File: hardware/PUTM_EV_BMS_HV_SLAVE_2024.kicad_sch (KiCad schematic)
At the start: 15 parts, among them J1 L_LTC_CONN, J1 R_LTC_CONN, J3 M80-5100442, J4 M80-5100442, T1 HM1236NL, T3 HM1236NL

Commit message: finished layout
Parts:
- added J5, J6: Conn_01x01_Pin, Connector_Wire:SolderWire-0.1sqmm_1x01_D0.4mm_OD1mm_Relief, symbol Connector:Conn_01x01_Pin
- C6, C7: Manufacturer_Part_Number (none) -> C0603C103J5RACTU; Mouser Part Number (none) -> 80-C0603C103J5R; Mouser Price/Stock (none) -> https://www.mouser.pl/ProductDetail/KEMET/C0603C103J5RACTU?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
- H1, H2, H3, H4: Manufacturer_Name (none) -> --; Manufacturer_Part_Number (none) -> --
- J1: value R_LTC_CONN -> IDC; Manufacturer_Part_Number (none) -> TST-110-01-T-D; Mouser Part Number (none) -> 200-TST11001TD; Mouser Price/Stock (none) -> https://www.mouser.pl/ProductDetail/Samtec/TST-110-01-T-D?q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
- J1: value L_LTC_CONN -> IDC; Manufacturer_Part_Number (none) -> TST-110-01-T-D; Mouser Part Number (none) -> 200-TST11001TD; Mouser Price/Stock (none) -> https://www.mouser.pl/ProductDetail/Samtec/TST-110-01-T-D?q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
- JP1: Manufacturer_Part_Number (none) -> --
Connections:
- net C11+: now also JP1.1 (A), S1.1
- net C2+: no longer JP1.1 (A), S1.1
- net at J3.1 (Pin_1): now also T1.5; no longer T1.4
- net at J3.3 (Pin_3): now also J3.4 (Pin_4), J5.1 (Pin_1); no longer T1.5
- net at T3.4: now also J4.2 (Pin_2); no longer J4.1 (Pin_1)
- net at T3.5: now also J4.1 (Pin_1); no longer J4.3 (Pin_3)
- net C2_SW+ renamed C11_SW+
- new net: J3.2 (Pin_2), T1.4
- new net: J4.3 (Pin_3), J4.4 (Pin_4), J6.1 (Pin_1)

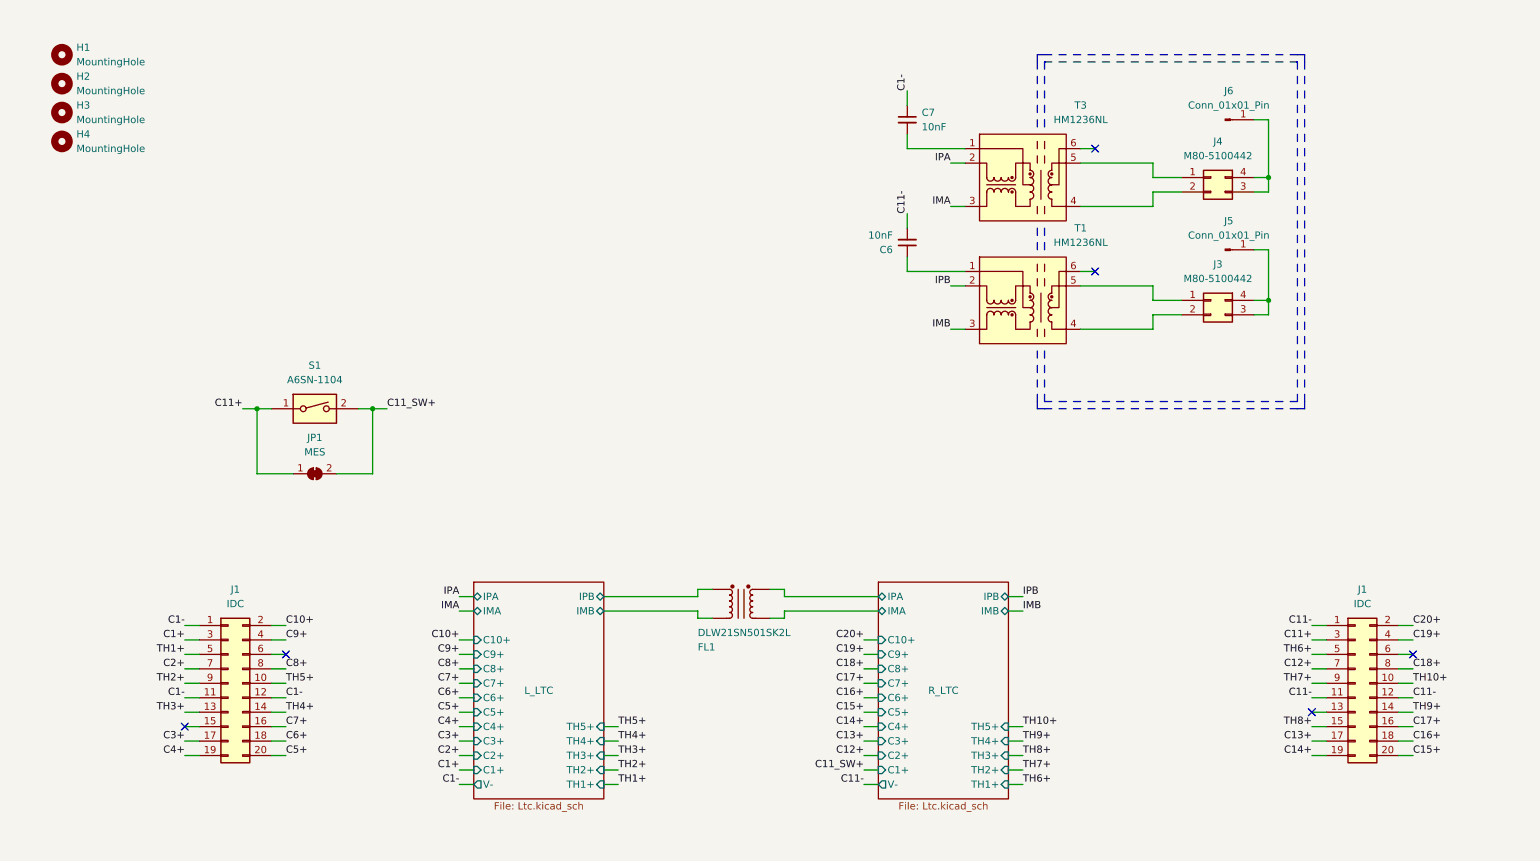
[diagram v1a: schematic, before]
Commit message: change from transformator to capacitive isolation between ltc, change ibias/icmp pin since they are incorrectly connected
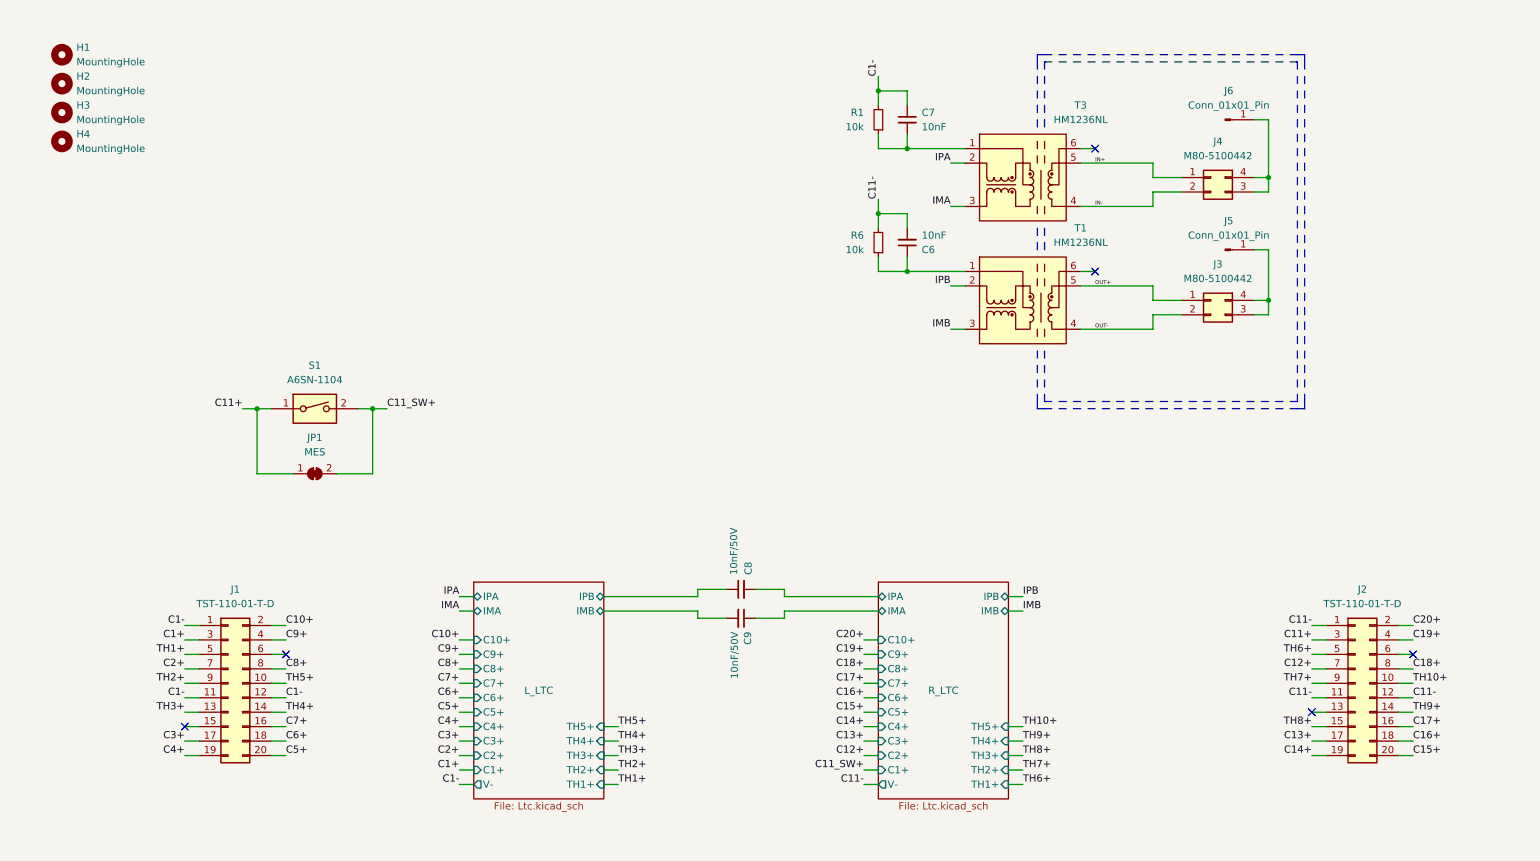
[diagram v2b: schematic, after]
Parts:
- removed FL1: DLW21SN501SK2L, Samacsys:DLW21SN121HQ2L, symbol dlw21sn501sk2l:DLW21SN501SK2L
- added C8, C9: 10nF/50V, Capacitor_SMD:C_0603_1608Metric, symbol PUTM_EV_BMS_HV_Slave_2021-rescue:C_Small-Device
- added R1, R6: 10k, Resistor_SMD:R_0603_1608Metric, symbol Device:R_Small
- J1: value IDC -> TST-110-01-T-D
- J2: renamed from J1; value IDC -> TST-110-01-T-D
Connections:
- net C1-: now also R1.2
- net C11-: now also R6.2
- net L_LTC/IMB: now also C9.2
- net L_LTC/IPB: now also C8.1
- net R_LTC/IMA: now also C9.1
- net R_LTC/IPA: now also C8.2
- net at C7.2, T3.1: now also R1.1
- net at C6.1, T1.1: now also R6.1
- net OUT+: now reaches J3.1 (Pin_1), T1.5
- net OUT-: now reaches J3.2 (Pin_2), T1.4
- net IN-: now reaches J4.2 (Pin_2), T3.4
- net IN+: now reaches J4.1 (Pin_1), T3.5

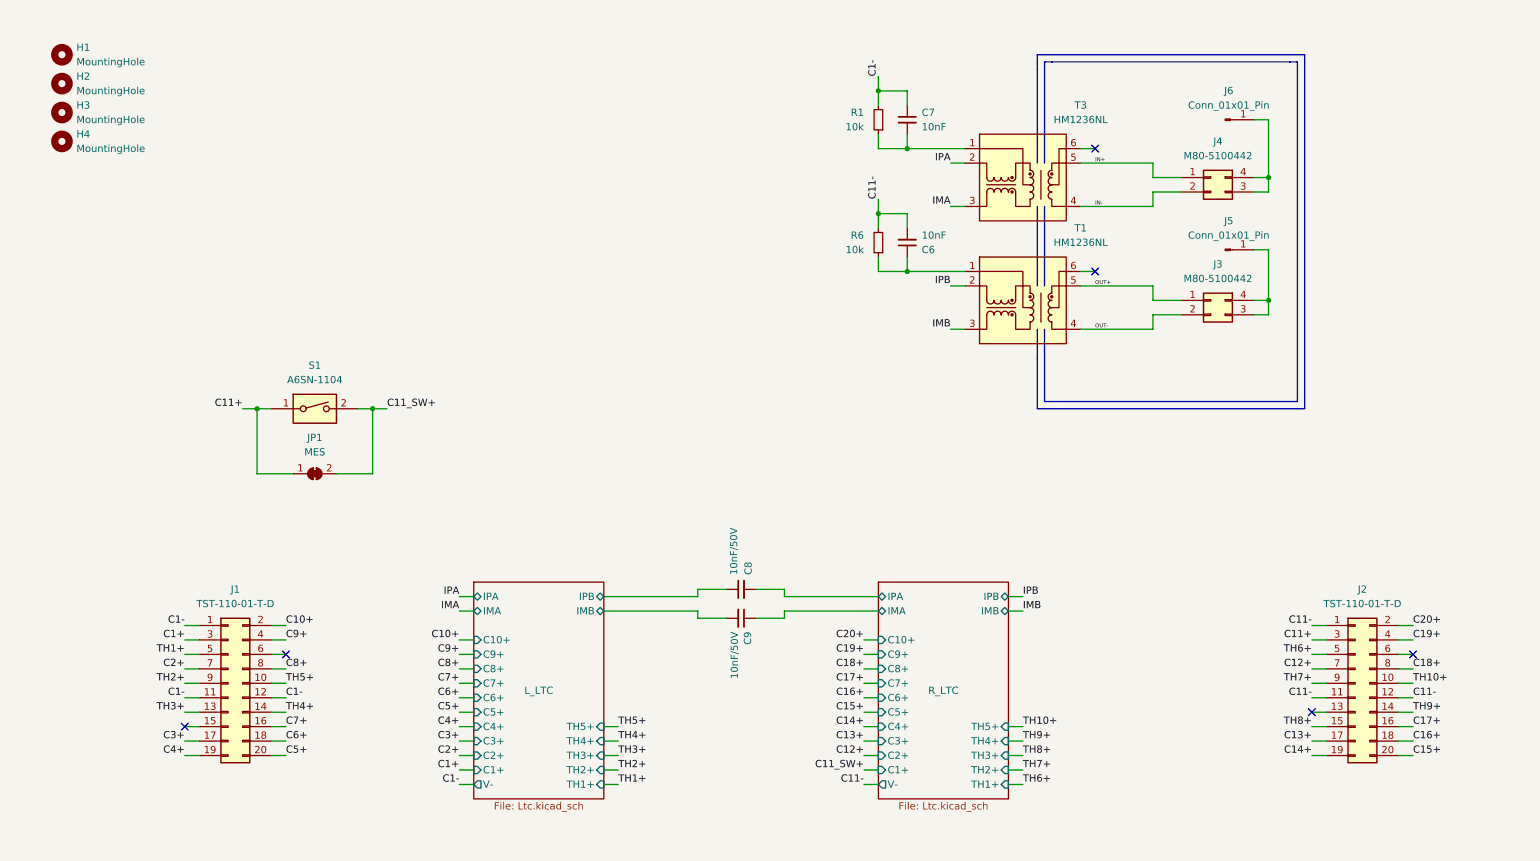
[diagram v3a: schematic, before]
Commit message: added temp disconnect, beautify schematic
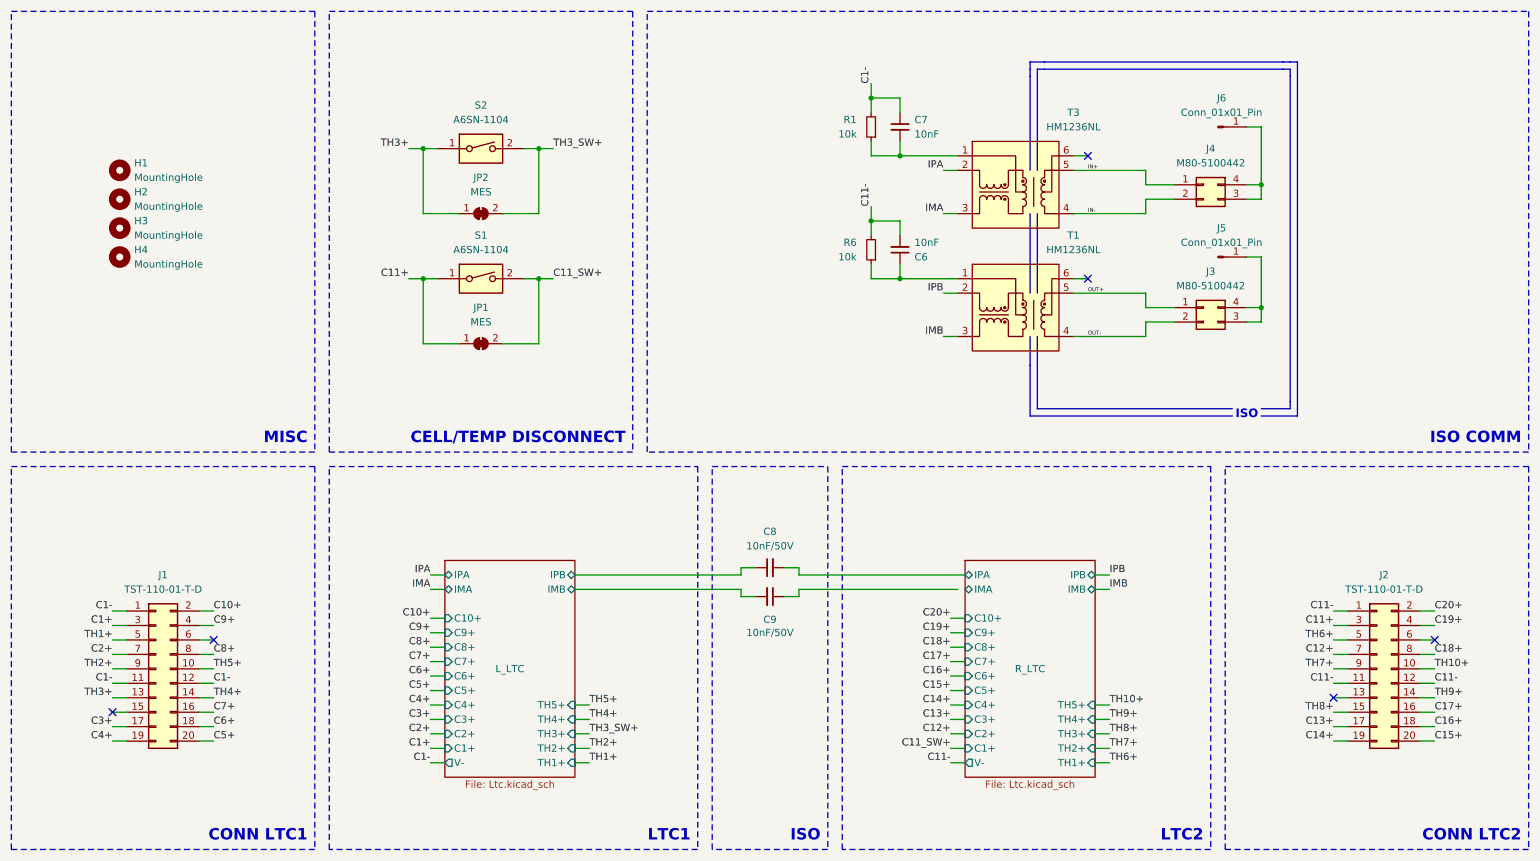
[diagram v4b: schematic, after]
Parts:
- added JP2: MES, Jumper:SolderJumper-2_P1.3mm_Bridged2Bar_RoundedPad1.0x1.5mm, symbol Jumper:SolderJumper_2_Bridged
- added S2: A6SN-1104, Samacsys:A6SN1104, symbol a6sn-1104:A6SN-1104
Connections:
- net R_LTC/IMA: no longer C9.1
- net TH3+: now also JP2.1 (A), S2.1
- new net TH3_SW+: JP2.2 (B), S2.2
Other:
- note added: "CELL/TEMP DISCONNECT"
- note added: "CONN LTC1"
- note added: "CONN LTC2"
- note added: "ISO"
- note added: "ISO COMM"
- note added: "LTC1"
- note added: "LTC2"
- note added: "MISC"
- moved on the sheet: C6, C7, C8, C9, H1, H2, H3, H4, J1, J2, J3, J4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

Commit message: replaced signal transformer with rated capacitors, made the design more general for future use
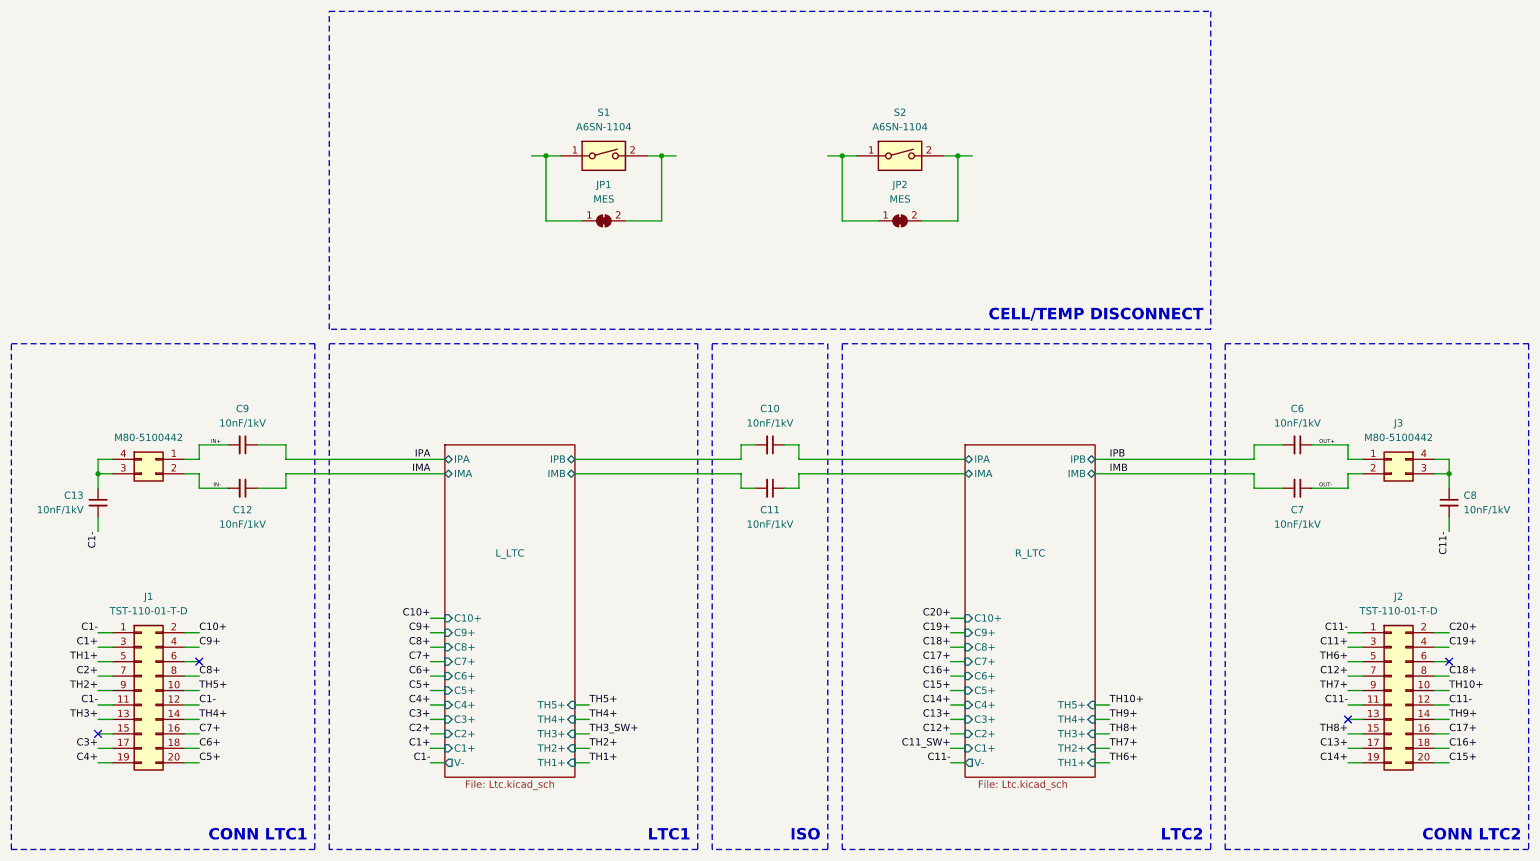
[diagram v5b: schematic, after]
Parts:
- removed C6, C7: 10nF, Capacitor_SMD:C_0603_1608Metric, symbol Device:C_Small
- removed C8, C9: 10nF/50V, Capacitor_SMD:C_0603_1608Metric, symbol PUTM_EV_BMS_HV_Slave_2021-rescue:C_Small-Device
- removed H1, H2, H3, H4: MountingHole, MountingHole:MountingHole_3.2mm_M3, symbol Mechanical:MountingHole
- removed J5, J6: Conn_01x01_Pin, Connector_Wire:SolderWire-0.1sqmm_1x01_D0.4mm_OD1mm_Relief, symbol Connector:Conn_01x01_Pin
- removed R1, R6: 10k, Resistor_SMD:R_0603_1608Metric, symbol Device:R_Small
- removed T1, T3: HM1236NL, Samacsys:HM1236NL, symbol hm1236nl:HM1236NL
- added C10, C11, C12, C13, C6, C7, C8, C9: 10nF/1kV, Capacitor_SMD:C_1206_3216Metric, symbol c2824c562jggacauto:C2824C562JGGACAUTO
- J1, J2: footprint Connector_IDC:IDC-Header_2x10_P2.54mm_Vertical -> Connector_IDC:IDC-Header_2x10_P2.54mm_Latch6.5mm_Vertical
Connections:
- net C1-: now also C13.2
- net C11+: no longer JP1.1 (A), S1.1
- net C11-: now also C8.2
- net C11_SW+: no longer JP1.2 (B), S1.2
- net IMA: now also C12.1
- net IMB: now also C7.2
- net IN+: now also C9.2
- net IN-: now also C12.2
- net IPA: now also C9.1
- net IPB: now also C6.2
- net L_LTC/IMB: now also C11.2
- net L_LTC/IPB: now also C10.2
- net OUT+: now also C6.1
- net OUT-: now also C7.1
- net R_LTC/IMA: now also C11.1
- net R_LTC/IPA: now also C10.1
- net TH3+: no longer JP2.1 (A), S2.1
- net TH3_SW+: no longer JP2.2 (B), S2.2
- net at J3.3 (Pin_3), J3.4 (Pin_4): now also C8.1
- net at J4.3 (Pin_3), J4.4 (Pin_4): now also C13.1
- new net: JP1.1 (A), S1.1
- new net: JP1.2 (B), S1.2
- new net: JP2.1 (A), S2.1
- new net: JP2.2 (B), S2.2
- no-connect marks 6 -> 4
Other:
- note removed: "ISO COMM"
- note removed: "MISC"
- moved on the sheet: J1, J2, J3, JP1, JP2, S1, S2
